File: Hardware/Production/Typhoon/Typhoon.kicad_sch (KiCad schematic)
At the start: 39 parts, among them J1 RBUS, U1 ESP32-S3, Y1 R940000171

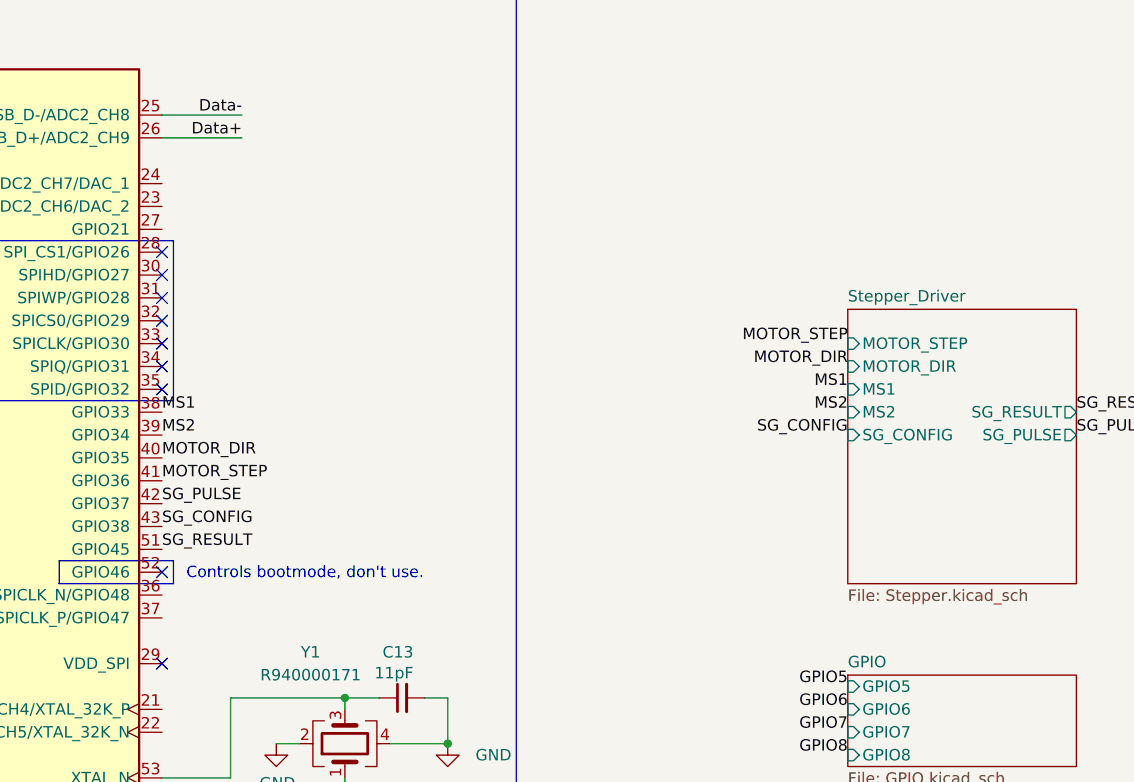
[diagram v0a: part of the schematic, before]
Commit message: Updated schematic, added mosfets to ENN and SPREAD pins of TMC2209 and connected INDEX, CLK, and VREF to GPIO pins
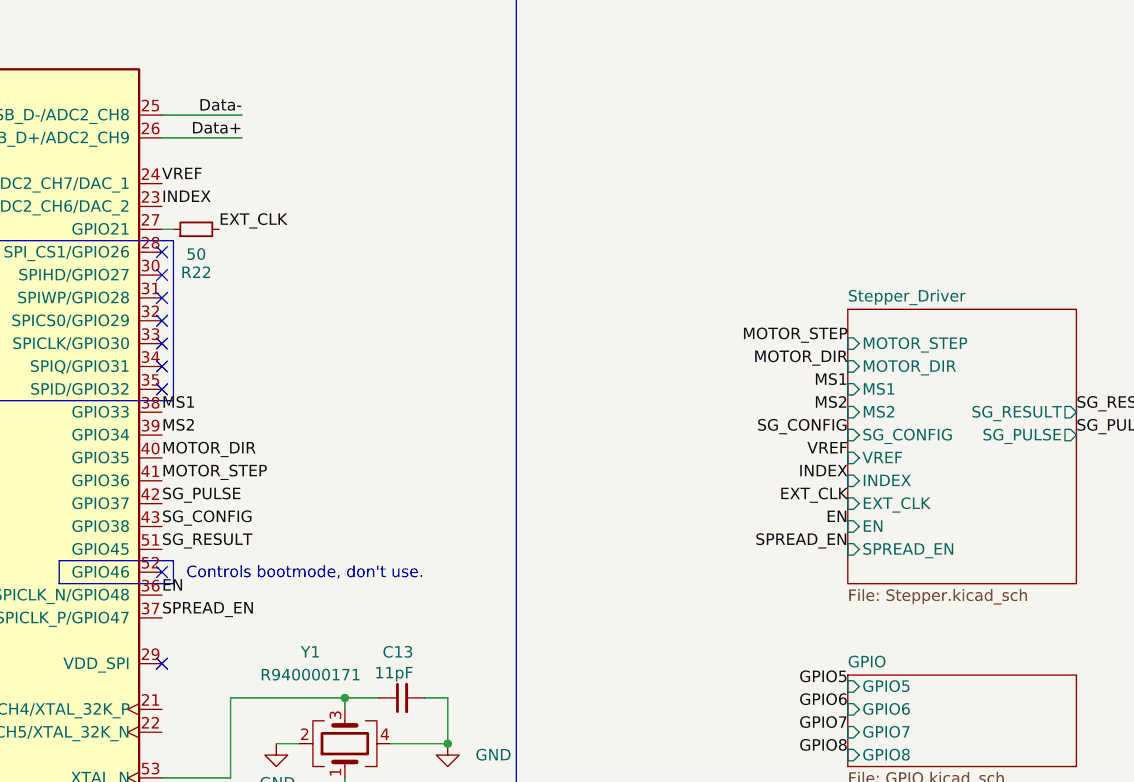
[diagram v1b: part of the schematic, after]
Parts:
- added R22: 50, Resistor_SMD:R_0402_1005Metric, symbol Device:R_Small
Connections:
- net INDEX: now reaches U1.23 (GPIO17/ADC2_CH6/DAC_2)
- net VREF: now reaches U1.24 (GPIO18/ADC2_CH7/DAC_1)
- net at U1.27 (GPIO21): now also R22.1
- net EN: now reaches U1.36 (SPICLK_N/GPIO48)
- net SPREAD_EN: now reaches U1.37 (SPICLK_P/GPIO47)
- new net EXT_CLK: R22.2
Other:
- sheet Stepper_Driver ports: added EN, EXT_CLK, INDEX, SPREAD_EN, VREF; removed none
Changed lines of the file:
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@@
 	(wire
 		(pts
+			(xy 135.89 74.93) (xy 137.16 74.93)
+		)
+		(stroke
+			(width 0)
+			(type default)
+		)
+	)
+	(wire
+		(pts
 			(xy 59.69 142.24) (xy 62.23 142.24)
 		)
@@
 		)
 	)
+	(label "VREF"
+		(at 135.89 69.85 0)
+		(fields_autoplaced yes)
+		(effects
+			(font
+				(size 1.27 1.27)
+			)
+			(justify left bottom)
+		)
+	)
 	(label "SG_RESULT"
 		(at 237.49 95.25 0)
@@
 		)
 	)
+	(label "EXT_CLK"
+		(at 212.09 105.41 180)
+		(fields_autoplaced yes)
+		(effects
+			(font
+				(size 1.27 1.27)
+			)
+			(justify right bottom)
+		)
+	)
 	(label "CAN+"
 		(at 115.57 185.42 0)
@@
 		)
 	)
+	(label "INDEX"
+		(at 135.89 72.39 0)
+		(fields_autoplaced yes)
+		(effects
+			(font
+				(size 1.27 1.27)
+			)
+			(justify left bottom)
+		)
+	)
+	(label "EN"
+		(at 135.89 115.57 0)
+		(fields_autoplaced yes)
+		(effects
+			(font
+				(size 1.27 1.27)
+			)
+			(justify left bottom)
+		)
+	)
+	(label "SPREAD_EN"
+		(at 135.89 118.11 0)
+		(fields_autoplaced yes)
+		(effects
+			(font
+				(size 1.27 1.27)
+			)
+			(justify left bottom)
+		)
+	)
 	(label "Data-"
 		(at 99.06 162.56 0)
@@
 		)
 	)
+	(label "EN"
+		(at 212.09 107.95 180)
+		(fields_autoplaced yes)
+		(effects
+			(font
+				(size 1.27 1.27)
+			)
+			(justify right bottom)
+		)
+	)
 	(label "TXD"
 		(at 30.48 54.61 0)
@@
 		)
 	)
+	(label "SPREAD_EN"
+		(at 212.09 110.49 180)
+		(fields_autoplaced yes)
+		(effects
+			(font
+				(size 1.27 1.27)
+			)
+			(justify right bottom)
+		)
+	)
 	(label "MOTOR_STEP"
 		(at 212.09 87.63 180)
@@
 		)
 	)
+	(label "INDEX"
+		(at 212.09 102.87 180)
+		(fields_autoplaced yes)
+		(effects
+			(font
+				(size 1.27 1.27)
+			)
+			(justify right bottom)
+		)
+	)
 	(label "CAN_RX"
 		(at 115.57 182.88 0)
@@
 		)
 	)
+	(label "VREF"
+		(at 212.09 100.33 180)
+		(fields_autoplaced yes)
+		(effects
+			(font
+				(size 1.27 1.27)
+			)
+			(justify right bottom)
+		)
+	)
 	(label "CAN-"
 		(at 115.57 187.96 0)
@@
 		)
 	)
+	(label "EXT_CLK"
+		(at 142.24 74.93 0)
+		(fields_autoplaced yes)
+		(effects
+			(font
+				(size 1.27 1.27)
+			)
+			(justify left bottom)
+		)
+	)
 	(label "GPIO7"
 		(at 69.85 87.63 180)
@@
 	)
 	(symbol
+		(lib_id "Device:R_Small")
+		(at 139.7 74.93 90)
+		(unit 1)
+		(exclude_from_sim no)
+		(in_bom yes)
+		(on_board yes)
+		(dnp no)
+		(property "Reference" "R22"
+			(at 139.7 79.756 90)
+			(effects
+				(font
+					(size 1.27 1.27)
+				)
+			)
+		)
+		(property "Value" "50"
+			(at 139.7 77.724 90)
+			(effects
+				(font
+					(size 1.27 1.27)
+				)
+			)
+		)
+		(property "Footprint" "Resistor_SMD:R_0402_1005Metric"
+			(at 139.7 74.93 0)
+			(effects
+				(font
+					(size 1.27 1.27)
+				)
+				(hide yes)
+			)
+		)
+		(property "Datasheet" "~"
+			(at 139.7 74.93 0)
+			(effects
+				(font
+					(size 1.27 1.27)
+				)
+				(hide yes)
+			)
+		)
+		(property "Description" "Resistor, small symbol"
+			(at 139.7 74.93 0)
+			(effects
+				(font
+					(size 1.27 1.27)
+				)
+				(hide yes)
+			)
+		)
+		(pin "2"
+		)
+		(pin "1"
+		)
+		(instances
+			(project ""
+				(path "/7db990e4-92e1-4f99-b4d2-435bbec1ba83"
+					(reference "R22")
+					(unit 1)
+				)
+			)
+		)
+	)
+	(symbol
 		(lib_id "Mechanical:MountingHole_Pad")
 		(at 262.89 30.48 0)
@@
 			)
 		)
+		(pin "VREF" input
+			(at 212.09 100.33 180)
+			(effects
+				(font
+					(size 1.27 1.27)
+				)
+				(justify left)
+			)
+		)
+		(pin "INDEX" input
+			(at 212.09 102.87 180)
+			(effects
+				(font
+					(size 1.27 1.27)
+				)
+				(justify left)
+			)
+		)
+		(pin "EXT_CLK" input
+			(at 212.09 105.41 180)
+			(effects
+				(font
+					(size 1.27 1.27)
+				)
+				(justify left)
+			)
+		)
+		(pin "EN" input
+			(at 212.09 107.95 180)
+			(effects
+				(font
+					(size 1.27 1.27)
+				)
+				(justify left)
+			)
+		)
+		(pin "SPREAD_EN" input
+			(at 212.09 110.49 180)
+			(effects
+				(font
+					(size 1.27 1.27)
+				)
+				(justify left)
+			)
+		)
